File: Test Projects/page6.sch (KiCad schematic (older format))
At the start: 24 parts, among them P13 CONN_01X08, P14 CONN_01X08, P15 CONN_01X08, P16 CONN_01X08, P17 CONN_01X08, P18 CONN_01X08, P19 CONN_01X08, P20 CONN_01X08, U18 SF-74HC595, U19 SF-74HC595, U20 SF-74HC595, U21 SF-74HC595, U22 SF-74HC595, U23 SF-74HC595, U24 SF-74HC595, U25 SF-74HC595

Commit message: Continued proto 1 layout
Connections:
- net +5V: now reaches C26.1, U18.16 (VCC)
- net +5V: now also C27.1, C28.1, C29.1, C30.1, C31.1, C32.1, C33.1, U19.16 (VCC), U20.16 (VCC), U21.16 (VCC), U22.16 (VCC), U23.16 (VCC), U24.16 (VCC), U25.16 (VCC)
- net GND: now reaches C26.2, U18.8 (GND)
- net GND: now also C27.2, C28.2, C29.2, C30.2, C31.2, C32.2, C33.2, U19.8 (GND), U20.8 (GND), U21.8 (GND), U22.8 (GND), U23.8 (GND), U24.8 (GND), U25.8 (GND)

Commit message: Moved to 10x5 size
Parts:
- renumbered C26 to C29, C27 to C30, C28 to C31, C29 to C32, C30 to C33, C31 to C34, C32 to C35, C33 to C36, P13 to P22, P14 to P23, P15 to P24, P16 to P25, P17 to P26, P18 to P27, P19 to P28, P20 to P29, U18 to U23, U19 to U24, U20 to U25, U21 to U26, U22 to U27, U23 to U28, U24 to U29, U25 to U30
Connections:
- net LEDSCLK renamed SD_LED_SCK
- net LEDSER renamed SD_LED_MOSI

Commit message: First major routing pass
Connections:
- net !LED_RST: now reaches U27.10 (SRCLR)
- net !LED_RST: now also U23.10 (SRCLR), U24.10 (SRCLR), U25.10 (SRCLR), U26.10 (SRCLR), U28.10 (SRCLR), U29.10 (SRCLR), U30.10 (SRCLR)
- net LEDLATCH renamed LED_LATCH
- net LEDOE renamed LED_OE
- net SD_LED_MOSI renamed SPI_MOSI
- net SD_LED_SCK renamed SPI_SCK
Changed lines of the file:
@@
 $EndComp
 Text GLabel 1250 3150 0    50   Input ~ 0
-LEDLATCH
+LED_LATCH
 Text GLabel 1250 3250 0    50   Input ~ 0
-LEDOE
+LED_OE
 $Comp
 L C C29
@@
 $EndComp
 Text GLabel 3750 3150 0    50   Input ~ 0
-LEDLATCH
+LED_LATCH
 Text GLabel 3750 3250 0    50   Input ~ 0
-LEDOE
+LED_OE
 $Comp
 L SF-74HC595 U29
@@
 $EndComp
 Text GLabel 6250 3150 0    50   Input ~ 0
-LEDLATCH
+LED_LATCH
 Text GLabel 6250 3250 0    50   Input ~ 0
-LEDOE
+LED_OE
 $Comp
 L SF-74HC595 U30
@@
 $EndComp
 Text GLabel 8750 3150 0    50   Input ~ 0
-LEDLATCH
+LED_LATCH
 Text GLabel 8750 3250 0    50   Input ~ 0
-LEDOE
+LED_OE
 $Comp
 L SF-74HC595 U23
@@
 $EndComp
 Text GLabel 1250 950  0    50   Input ~ 0
-SD_LED_MOSI
-Text GLabel 1250 1150 0    50   Input ~ 0
-SD_LED_SCK
+SPI_MOSI
 Text GLabel 1250 1450 0    50   Input ~ 0
-LEDLATCH
+LED_LATCH
 Text GLabel 1250 1550 0    50   Input ~ 0
-LEDOE
+LED_OE
 $Comp
 L SF-74HC595 U24
@@
 $EndComp
 Text GLabel 3750 1450 0    50   Input ~ 0
-LEDLATCH
+LED_LATCH
 Text GLabel 3750 1550 0    50   Input ~ 0
-LEDOE
+LED_OE
 $Comp
 L SF-74HC595 U25
@@
 $EndComp
 Text GLabel 6250 1450 0    50   Input ~ 0
-LEDLATCH
+LED_LATCH
 Text GLabel 6250 1550 0    50   Input ~ 0
-LEDOE
+LED_OE
 $Comp
 L SF-74HC595 U26
@@
 $EndComp
 Text GLabel 8750 1450 0    50   Input ~ 0
-LEDLATCH
+LED_LATCH
 Text GLabel 8750 1550 0    50   Input ~ 0
-LEDOE
+LED_OE
 $Comp
 L SF-74HC595 U24
@@
 $EndComp
 $Comp
-L +5V #PWR62
+L +5V #PWR071
 U 1 1 568A1F71
 P 1750 4800
-F 0 "#PWR62" H 1750 4650 50  0001 C CNN
+F 0 "#PWR071" H 1750 4650 50  0001 C CNN
 F 1 "+5V" H 1750 4940 50  0000 C CNN
 F 2 "" H 1750 4800 50  0000 C CNN
@@
 	8200 2650 8800 2650
 $Comp
-L GND #PWR63
+L GND #PWR072
 U 1 1 568A29A6
 P 1750 6100
-F 0 "#PWR63" H 1750 5850 50  0001 C CNN
+F 0 "#PWR072" H 1750 5850 50  0001 C CNN
 F 1 "GND" H 1750 5950 50  0000 C CNN
 F 2 "" H 1750 6100 50  0000 C CNN
@@
 $EndComp
 $Comp
-L GND #PWR65
+L GND #PWR073
 U 1 1 568A2A18
 P 2550 6100
-F 0 "#PWR65" H 2550 5850 50  0001 C CNN
+F 0 "#PWR073" H 2550 5850 50  0001 C CNN
 F 1 "GND" H 2550 5950 50  0000 C CNN
 F 2 "" H 2550 6100 50  0000 C CNN
@@
 $EndComp
 $Comp
-L GND #PWR67
+L GND #PWR074
 U 1 1 568A2A83
 P 3350 6100
-F 0 "#PWR67" H 3350 5850 50  0001 C CNN
+F 0 "#PWR074" H 3350 5850 50  0001 C CNN
 F 1 "GND" H 3350 5950 50  0000 C CNN
 F 2 "" H 3350 6100 50  0000 C CNN
@@
 $EndComp
 $Comp
-L GND #PWR69
+L GND #PWR075
 U 1 1 568A2A89
 P 4150 6100
-F 0 "#PWR69" H 4150 5850 50  0001 C CNN
+F 0 "#PWR075" H 4150 5850 50  0001 C CNN
 F 1 "GND" H 4150 5950 50  0000 C CNN
 F 2 "" H 4150 6100 50  0000 C CNN
@@
 $EndComp
 $Comp
-L GND #PWR71
+L GND #PWR076
 U 1 1 568A2B8F
 P 4950 6100
-F 0 "#PWR71" H 4950 5850 50  0001 C CNN
+F 0 "#PWR076" H 4950 5850 50  0001 C CNN
 F 1 "GND" H 4950 5950 50  0000 C CNN
 F 2 "" H 4950 6100 50  0000 C CNN
@@
 $EndComp
 $Comp
-L GND #PWR73
+L GND #PWR077
 U 1 1 568A2B95
 P 5750 6100
-F 0 "#PWR73" H 5750 5850 50  0001 C CNN
+F 0 "#PWR077" H 5750 5850 50  0001 C CNN
 F 1 "GND" H 5750 5950 50  0000 C CNN
 F 2 "" H 5750 6100 50  0000 C CNN
@@
 $EndComp
 $Comp
-L GND #PWR75
+L GND #PWR078
 U 1 1 568A2B9B
 P 6550 6100
-F 0 "#PWR75" H 6550 5850 50  0001 C CNN
+F 0 "#PWR078" H 6550 5850 50  0001 C CNN
 F 1 "GND" H 6550 5950 50  0000 C CNN
 F 2 "" H 6550 6100 50  0000 C CNN
@@
 $EndComp
 $Comp
-L GND #PWR77
+L GND #PWR079
 U 1 1 568A2BA1
 P 7350 6100
-F 0 "#PWR77" H 7350 5850 50  0001 C CNN
+F 0 "#PWR079" H 7350 5850 50  0001 C CNN
 F 1 "GND" H 7350 5950 50  0000 C CNN
 F 2 "" H 7350 6100 50  0000 C CNN
@@
 $EndComp
 $Comp
-L +5V #PWR64
+L +5V #PWR080
 U 1 1 568A2BE7
 P 2550 4800
-F 0 "#PWR64" H 2550 4650 50  0001 C CNN
+F 0 "#PWR080" H 2550 4650 50  0001 C CNN
 F 1 "+5V" H 2550 4940 50  0000 C CNN
 F 2 "" H 2550 4800 50  0000 C CNN
@@
 $EndComp
 $Comp
-L +5V #PWR66
+L +5V #PWR081
 U 1 1 568A2C52
 P 3350 4800
-F 0 "#PWR66" H 3350 4650 50  0001 C CNN
+F 0 "#PWR081" H 3350 4650 50  0001 C CNN
 F 1 "+5V" H 3350 4940 50  0000 C CNN
 F 2 "" H 3350 4800 50  0000 C CNN
@@
 $EndComp
 $Comp
-L +5V #PWR68
+L +5V #PWR082
 U 1 1 568A2CBD
 P 4150 4800
-F 0 "#PWR68" H 4150 4650 50  0001 C CNN
+F 0 "#PWR082" H 4150 4650 50  0001 C CNN
 F 1 "+5V" H 4150 4940 50  0000 C CNN
 F 2 "" H 4150 4800 50  0000 C CNN
@@
 $EndComp
 $Comp
-L +5V #PWR70
+L +5V #PWR083
 U 1 1 568A2D28
 P 4950 4800
-F 0 "#PWR70" H 4950 4650 50  0001 C CNN
+F 0 "#PWR083" H 4950 4650 50  0001 C CNN
 F 1 "+5V" H 4950 4940 50  0000 C CNN
 F 2 "" H 4950 4800 50  0000 C CNN
@@
 $EndComp
 $Comp
-L +5V #PWR72
+L +5V #PWR084
 U 1 1 568A2D93
 P 5750 4800
-F 0 "#PWR72" H 5750 4650 50  0001 C CNN
+F 0 "#PWR084" H 5750 4650 50  0001 C CNN
 F 1 "+5V" H 5750 4940 50  0000 C CNN
 F 2 "" H 5750 4800 50  0000 C CNN
@@
 $EndComp
 $Comp
-L +5V #PWR74
+L +5V #PWR085
 U 1 1 568A2DFE
 P 6550 4800
-F 0 "#PWR74" H 6550 4650 50  0001 C CNN
+F 0 "#PWR085" H 6550 4650 50  0001 C CNN
 F 1 "+5V" H 6550 4940 50  0000 C CNN
 F 2 "" H 6550 4800 50  0000 C CNN
@@
 $EndComp
 $Comp
-L +5V #PWR76
+L +5V #PWR086
 U 1 1 568A2E69
 P 7350 4800
-F 0 "#PWR76" H 7350 4650 50  0001 C CNN
+F 0 "#PWR086" H 7350 4650 50  0001 C CNN
 F 1 "+5V" H 7350 4940 50  0000 C CNN
 F 2 "" H 7350 4800 50  0000 C CNN
@@
 	4150 5900 4150 6100
 Connection ~ 4150 6000
+Text GLabel 8750 2850 0    50   Input ~ 0
+SPI_SCK
+Text GLabel 1250 2950 0    50   Input ~ 0
+!LED_RST
+Text GLabel 1250 1150 0    50   Input ~ 0
+SPI_SCK
 Text GLabel 3750 1150 0    50   Input ~ 0
-SD_LED_SCK
+SPI_SCK
 Text GLabel 6250 1150 0    50   Input ~ 0
-SD_LED_SCK
+SPI_SCK
 Text GLabel 8750 1150 0    50   Input ~ 0
-SD_LED_SCK
-Text GLabel 8750 2850 0    50   Input ~ 0
-SD_LED_SCK
+SPI_SCK
 Text GLabel 6250 2850 0    50   Input ~ 0
-SD_LED_SCK
+SPI_SCK
 Text GLabel 3750 2850 0    50   Input ~ 0
-SD_LED_SCK
+SPI_SCK
 Text GLabel 1250 2850 0    50   Input ~ 0
-SD_LED_SCK
+SPI_SCK
+Wire Wire Line
+	1250 2950 1300 2950
+Text GLabel 1250 1250 0    50   Input ~ 0
+!LED_RST
+Wire Wire Line
+	1250 1250 1300 1250
+Text GLabel 3750 1250 0    50   Input ~ 0
+!LED_RST
+Wire Wire Line
+	3750 1250 3800 1250
+Text GLabel 3750 2950 0    50   Input ~ 0
+!LED_RST
+Wire Wire Line
+	3750 2950 3800 2950
+Text GLabel 8750 1250 0    50   Input ~ 0
+!LED_RST
+Wire Wire Line
+	8750 1250 8800 1250
+Text GLabel 6250 1250 0    50   Input ~ 0
+!LED_RST
+Wire Wire Line
+	6250 1250 6300 1250
+Text GLabel 8750 2950 0    50   Input ~ 0
+!LED_RST
+Wire Wire Line
+	8750 2950 8800 2950
+Text GLabel 6250 2950 0    50   Input ~ 0
+!LED_RST
+Wire Wire Line
+	6250 2950 6300 2950
 $EndSCHEMATC

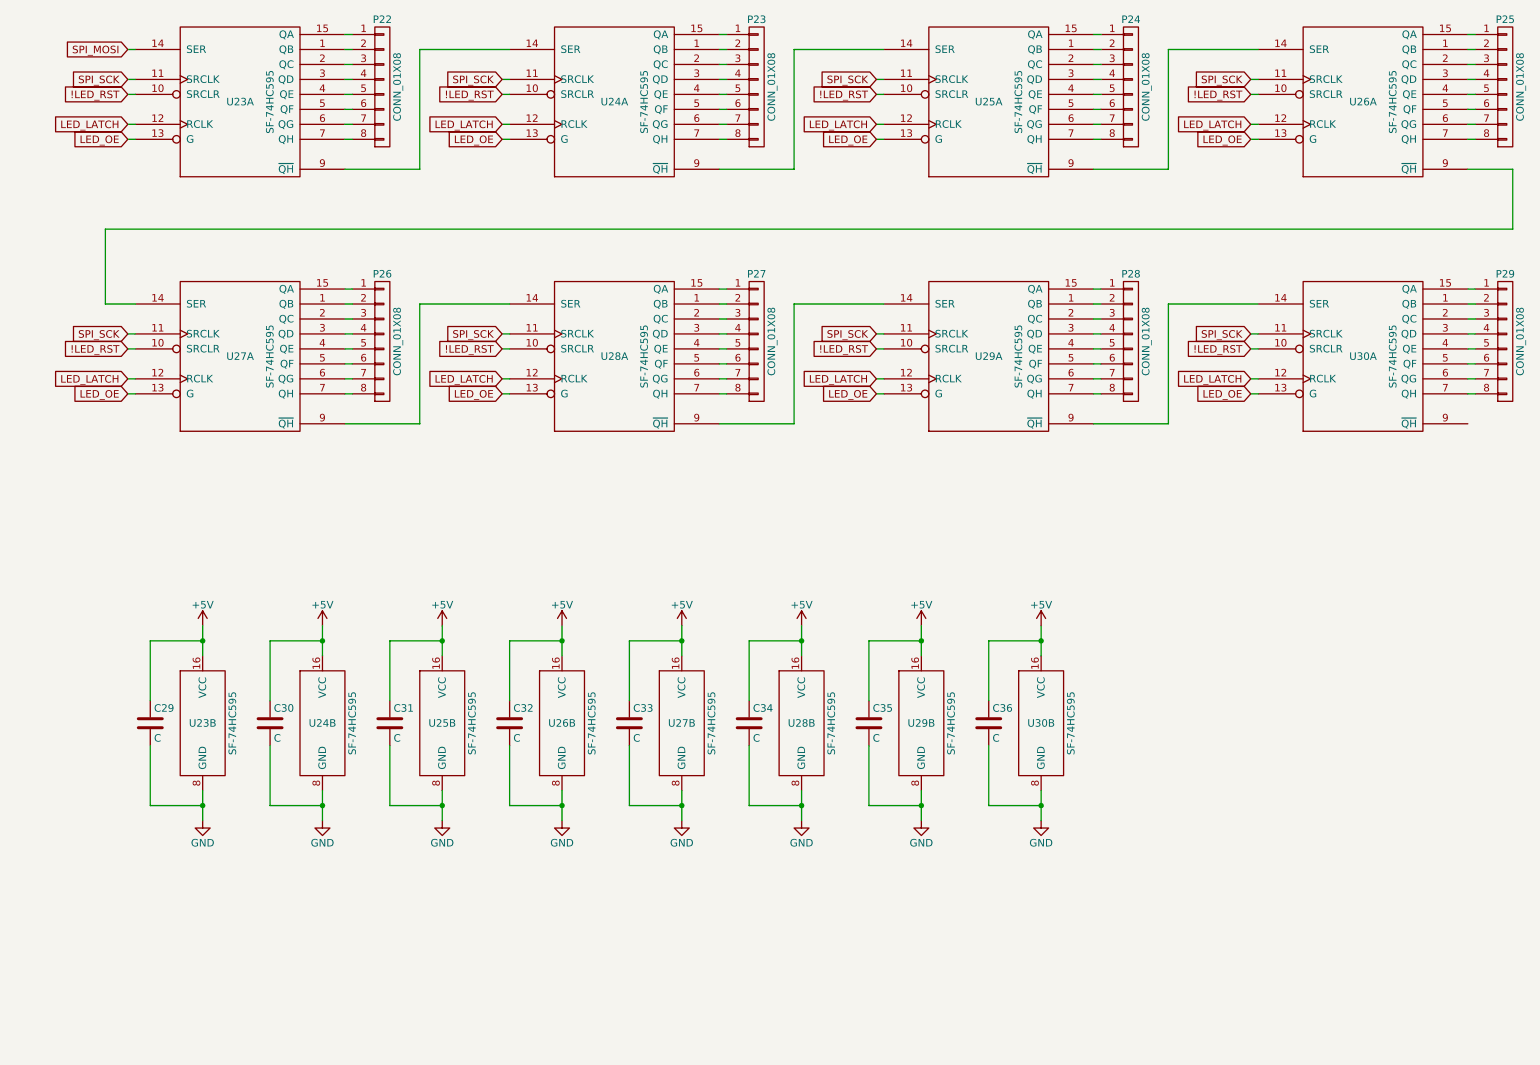
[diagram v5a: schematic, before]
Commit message: Added holes, moved layout
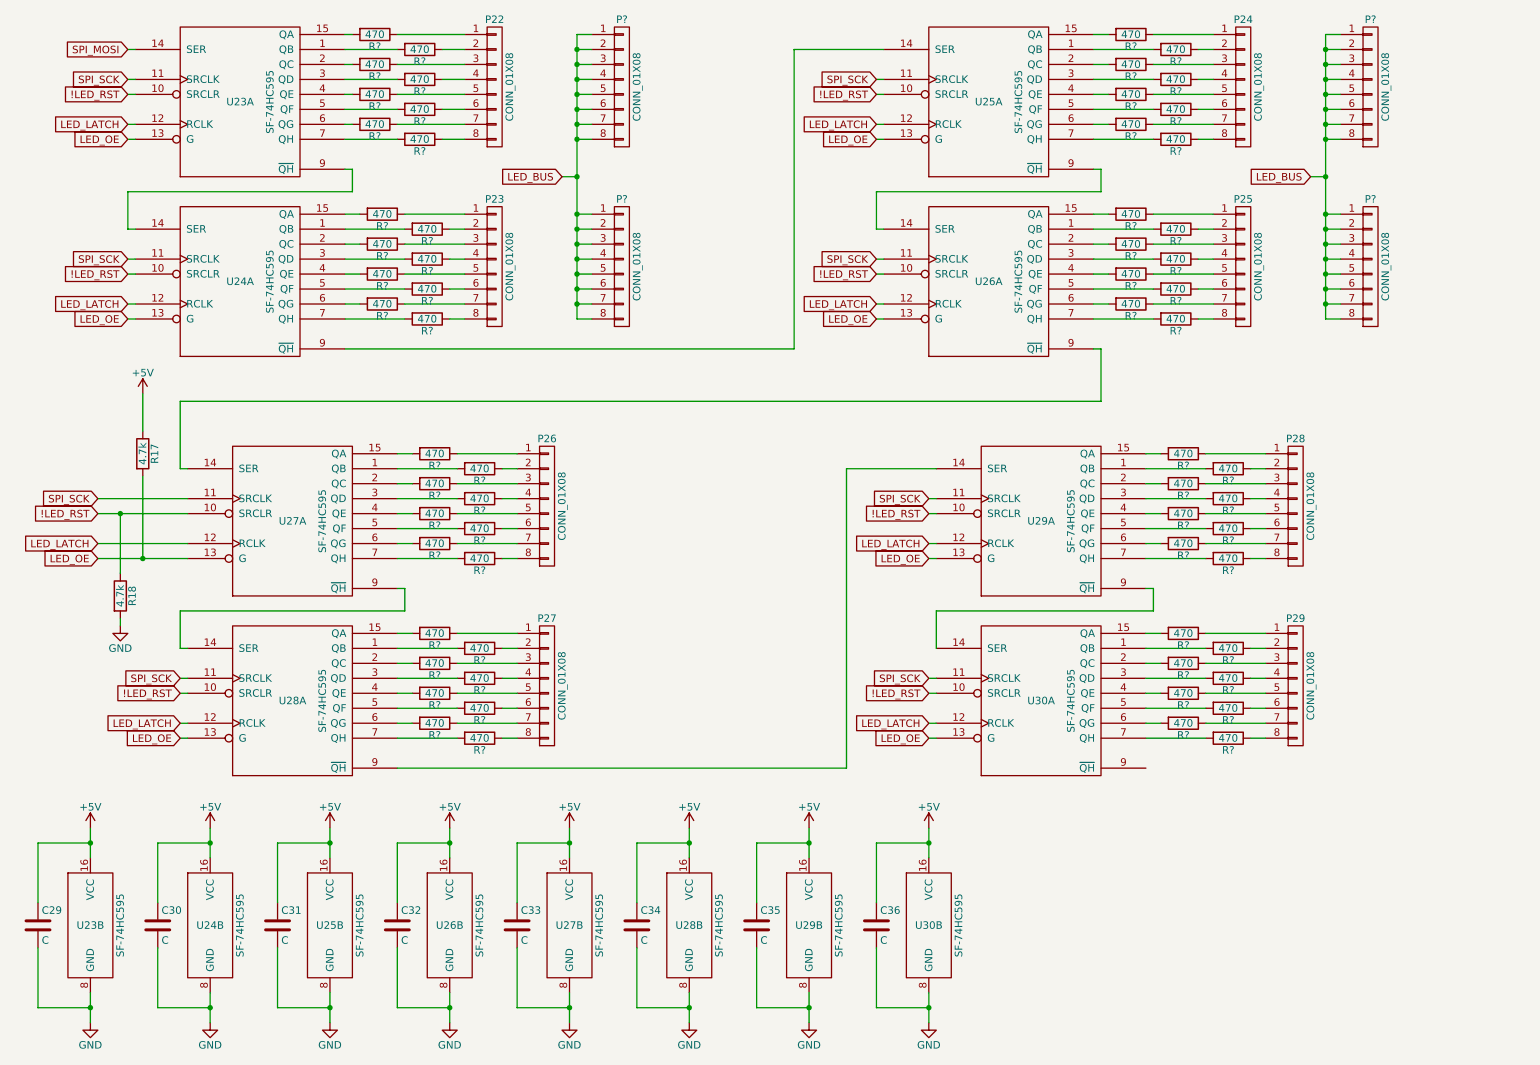
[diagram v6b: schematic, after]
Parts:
- added P? (x4): CONN_01X08, Pin_Headers:Pin_Header_Straight_1x08, symbol CONN_01X08
- added R17, R18: 4.7k, Resistors_SMD:R_0603, symbol R
- added R? (x64): 470, symbol R
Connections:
- net !LED_RST: now also R18.1
- net +5V: now also R17.1
- net GND: now also R18.2
- net LED_OE: now also R17.2
- net at U27.1 (QB): now also R?.2; no longer P26.2 (P2)
- net at U27.15 (QA): now also R?.2; no longer P26.1 (P1)
- net at U27.2 (QC): now also R?.2; no longer P26.3 (P3)
- net at U27.3 (QD): now also R?.2; no longer P26.4 (P4)
- net at U27.4 (QE): now also R?.2; no longer P26.5 (P5)
- net at U27.5 (QF): now also R?.2; no longer P26.6 (P6)
- net at U27.6 (QG): now also R?.2; no longer P26.7 (P7)
- net at U27.7 (QH): now also R?.2; no longer P26.8 (P8)
- net at U28.1 (QB): now also R?.2; no longer P27.2 (P2)
- net at U28.15 (QA): now also R?.2; no longer P27.1 (P1)
- net at U28.2 (QC): now also R?.2; no longer P27.3 (P3)
- net at U28.3 (QD): now also R?.2; no longer P27.4 (P4)
- net at U28.4 (QE): now also R?.2; no longer P27.5 (P5)
- net at U28.5 (QF): now also R?.2; no longer P27.6 (P6)
- net at U28.6 (QG): now also R?.2; no longer P27.7 (P7)
- net at U28.7 (QH): now also R?.2; no longer P27.8 (P8)
- net at U29.1 (QB): now also R?.2; no longer P28.2 (P2)
- net at U29.15 (QA): now also R?.2; no longer P28.1 (P1)
- net at U29.2 (QC): now also R?.2; no longer P28.3 (P3)
- net at U29.3 (QD): now also R?.2; no longer P28.4 (P4)
- net at U29.4 (QE): now also R?.2; no longer P28.5 (P5)
- net at U29.5 (QF): now also R?.2; no longer P28.6 (P6)
- net at U29.6 (QG): now also R?.2; no longer P28.7 (P7)
- net at U29.7 (QH): now also R?.2; no longer P28.8 (P8)
- net at U30.1 (QB): now also R?.2; no longer P29.2 (P2)
- net at U30.15 (QA): now also R?.2; no longer P29.1 (P1)
- net at U30.2 (QC): now also R?.2; no longer P29.3 (P3)
- net at U30.3 (QD): now also R?.2; no longer P29.4 (P4)
- net at U30.4 (QE): now also R?.2; no longer P29.5 (P5)
- net at U30.5 (QF): now also R?.2; no longer P29.6 (P6)
- net at U30.6 (QG): now also R?.2; no longer P29.7 (P7)
- net at U30.7 (QH): now also R?.2; no longer P29.8 (P8)
- net at U23.1 (QB): now also R?.2; no longer P22.2 (P2)
- net at U23.15 (QA): now also R?.2; no longer P22.1 (P1)
- net at U23.2 (QC): now also R?.2; no longer P22.3 (P3)
- net at U23.3 (QD): now also R?.2; no longer P22.4 (P4)
- net at U23.4 (QE): now also R?.2; no longer P22.5 (P5)
- net at U23.5 (QF): now also R?.2; no longer P22.6 (P6)
- net at U23.6 (QG): now also R?.2; no longer P22.7 (P7)
- net at U23.7 (QH): now also R?.2; no longer P22.8 (P8)
- net at U24.1 (QB): now also R?.2; no longer P23.2 (P2)
- net at U24.15 (QA): now also R?.2; no longer P23.1 (P1)
- net at U24.2 (QC): now also R?.2; no longer P23.3 (P3)
- net at U24.3 (QD): now also R?.2; no longer P23.4 (P4)
- net at U24.4 (QE): now also R?.2; no longer P23.5 (P5)
- net at U24.5 (QF): now also R?.2; no longer P23.6 (P6)
- net at U24.6 (QG): now also R?.2; no longer P23.7 (P7)
- net at U24.7 (QH): now also R?.2; no longer P23.8 (P8)
- net at U25.1 (QB): now also R?.2; no longer P24.2 (P2)
- net at U25.15 (QA): now also R?.2; no longer P24.1 (P1)
- net at U25.2 (QC): now also R?.2; no longer P24.3 (P3)
- net at U25.3 (QD): now also R?.2; no longer P24.4 (P4)
- net at U25.4 (QE): now also R?.2; no longer P24.5 (P5)
- net at U25.5 (QF): now also R?.2; no longer P24.6 (P6)
- net at U25.6 (QG): now also R?.2; no longer P24.7 (P7)
- net at U25.7 (QH): now also R?.2; no longer P24.8 (P8)
- net at U26.1 (QB): now also R?.2; no longer P25.2 (P2)
- net at U26.15 (QA): now also R?.2; no longer P25.1 (P1)
- net at U26.2 (QC): now also R?.2; no longer P25.3 (P3)
- net at U26.3 (QD): now also R?.2; no longer P25.4 (P4)
- net at U26.4 (QE): now also R?.2; no longer P25.5 (P5)
- net at U26.5 (QF): now also R?.2; no longer P25.6 (P6)
- net at U26.6 (QG): now also R?.2; no longer P25.7 (P7)
- net at U26.7 (QH): now also R?.2; no longer P25.8 (P8)
- new net: P26.1 (P1), R?.1
- new net: P26.2 (P2), R?.1
- new net: P26.3 (P3), R?.1
- new net: P26.4 (P4), R?.1
- new net: P26.5 (P5), R?.1
- new net: P26.6 (P6), R?.1
- new net: P26.7 (P7), R?.1
- new net: P26.8 (P8), R?.1
- new net: P27.1 (P1), R?.1
- new net: P27.2 (P2), R?.1
- new net: P27.3 (P3), R?.1
- new net: P27.4 (P4), R?.1
- new net: P27.5 (P5), R?.1
- new net: P27.6 (P6), R?.1
- new net: P27.7 (P7), R?.1
- new net: P27.8 (P8), R?.1
- new net: P28.1 (P1), R?.1
- new net: P28.2 (P2), R?.1
- new net: P28.3 (P3), R?.1
- new net: P28.4 (P4), R?.1
- new net: P28.5 (P5), R?.1
- new net: P28.6 (P6), R?.1
- new net: P28.7 (P7), R?.1
- new net: P28.8 (P8), R?.1
- new net: P29.1 (P1), R?.1
- new net: P29.2 (P2), R?.1
- new net: P29.3 (P3), R?.1
- new net: P29.4 (P4), R?.1
- new net: P29.5 (P5), R?.1
- new net: P29.6 (P6), R?.1
- new net: P29.7 (P7), R?.1
- new net: P29.8 (P8), R?.1
- new net: P22.1 (P1), R?.1
- new net: P22.2 (P2), R?.1
- new net: P22.3 (P3), R?.1
- new net: P22.4 (P4), R?.1
- new net: P22.5 (P5), R?.1
- new net: P22.6 (P6), R?.1
- new net: P22.7 (P7), R?.1
- new net: P22.8 (P8), R?.1
- new net: P23.1 (P1), R?.1
- new net: P23.2 (P2), R?.1
- new net: P23.3 (P3), R?.1
- new net: P23.4 (P4), R?.1
- new net: P23.5 (P5), R?.1
- new net: P23.6 (P6), R?.1
- new net: P23.7 (P7), R?.1
- new net: P23.8 (P8), R?.1
- new net: P24.1 (P1), R?.1
- new net: P24.2 (P2), R?.1
- new net: P24.3 (P3), R?.1
- new net: P24.4 (P4), R?.1
- new net: P24.5 (P5), R?.1
- new net: P24.6 (P6), R?.1
- new net: P24.7 (P7), R?.1
- new net: P24.8 (P8), R?.1
- new net: P25.1 (P1), R?.1
- new net: P25.2 (P2), R?.1
- new net: P25.3 (P3), R?.1
- new net: P25.4 (P4), R?.1
- new net: P25.5 (P5), R?.1
- new net: P25.6 (P6), R?.1
- new net: P25.7 (P7), R?.1
- new net: P25.8 (P8), R?.1
- new net LED_BUS: P?.1 (P1), P?.1 (P1), P?.1 (P1), P?.1 (P1), P?.2 (P2), P?.2 (P2), P?.2 (P2), P?.2 (P2), P?.3 (P3), P?.3 (P3), P?.3 (P3), P?.3 (P3), P?.4 (P4), P?.4 (P4), P?.4 (P4), P?.4 (P4), P?.5 (P5), P?.5 (P5), P?.5 (P5), P?.5 (P5), P?.6 (P6), P?.6 (P6), P?.6 (P6), P?.6 (P6), P?.7 (P7), P?.7 (P7), P?.7 (P7), P?.7 (P7), P?.8 (P8), P?.8 (P8), P?.8 (P8), P?.8 (P8)
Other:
- moved on the sheet: C29, C30, C31, C32, C33, C34, C35, C36, P22, P23, P24, P25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

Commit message: Routing, 15%
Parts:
- added P78, P79, P80, P81: CONN_01X08, Pin_Headers:Pin_Header_Straight_1x08, symbol CONN_01X08
- added P87, P88: CONN_01X01, SparkFun-Footprints:PTH_LUG_.05, symbol CONN_01X01
- R31, R32, R33, R34, R35, R36, R37, R38, R39, R40, R41, R42, R43, R44, R45, R46, R47, R48, R49, R50, R51, R52, R53, R54, R55, R56, R57, R58, R59, R60, R61, R62, R63, R64, R65, R66, R67, R68, R69, R70, R71, R72, R73, R74, R75, R76, R77, R78, R79, R80, R81, R82, R83, R84, R85, R86, R87, R88, R89, R90, R91, R92, R93, R94: renamed from R?; footprint (none) -> Resistors_SMD:R_0603
- gave numbers to parts that had none: 4
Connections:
- net LED_BUS: now also P78.1 (P1), P78.2 (P2), P78.3 (P3), P78.4 (P4), P78.5 (P5), P78.6 (P6), P78.7 (P7), P78.8 (P8), P79.1 (P1), P79.2 (P2), P79.3 (P3), P79.4 (P4), P79.5 (P5), P79.6 (P6), P79.7 (P7), P79.8 (P8), P80.1 (P1), P80.2 (P2), P80.3 (P3), P80.4 (P4), P80.5 (P5), P80.6 (P6), P80.7 (P7), P80.8 (P8), P81.1 (P1), P81.2 (P2), P81.3 (P3), P81.4 (P4), P81.5 (P5), P81.6 (P6), P81.7 (P7), P81.8 (P8), P87.1 (P1), P88.1 (P1)
